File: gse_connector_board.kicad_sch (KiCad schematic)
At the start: 19 parts, among them J1 arming_connector, J2 gse_com_connector, J3 chg_connector, U4 L7805, U7 ISO1044BD, U9 MCP2562-E-SN

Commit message: wip
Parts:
- removed BUS1: 43045-0800, Connector_Molex:Molex_Micro-Fit_3.0_43045-0800_2x04_P3.00mm_Horizontal, symbol Connector_Generic:Conn_02x04_Top_Bottom
- removed H3: MountingHole_Pad, MountingHole:MountingHole_3.2mm_M3_DIN965_Pad, symbol Mechanical:MountingHole_Pad
- added J4: Conn_02x03_Top_Bottom, Connector_Molex:Molex_Micro-Fit_3.0_43045-0600_2x03_P3.00mm_Horizontal, symbol Connector_Generic:Conn_02x03_Top_Bottom
- added J5: Conn_02x02_Top_Bottom, Connector_Molex:Molex_Micro-Fit_3.0_43045-0400_2x02_P3.00mm_Horizontal, symbol Connector_Generic:Conn_02x02_Top_Bottom
- JP4: footprint Connector_PinHeader_1.27mm:PinHeader_1x02_P1.27mm_Vertical -> Jumper:SolderJumper-2_P1.3mm_Bridged_RoundedPad1.0x1.5mm
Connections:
- net supply is gone; now on net main_voltage: J1.1 (Pin_1)
- net CAN_1+: now also J4.6 (Pin_6)
- net CAN_1-: now also J4.3 (Pin_3)
- net CHG: now also J4.4 (Pin_4)
- net GND: now also J4.1 (Pin_1), J4.2 (Pin_2)
- net arm: now also J5.3 (Pin_3), J5.4 (Pin_4)
- net disarm: now also J5.1 (Pin_1), J5.2 (Pin_2)
- net main_voltage: now also J4.5 (Pin_5)
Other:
- note removed: "critical can"

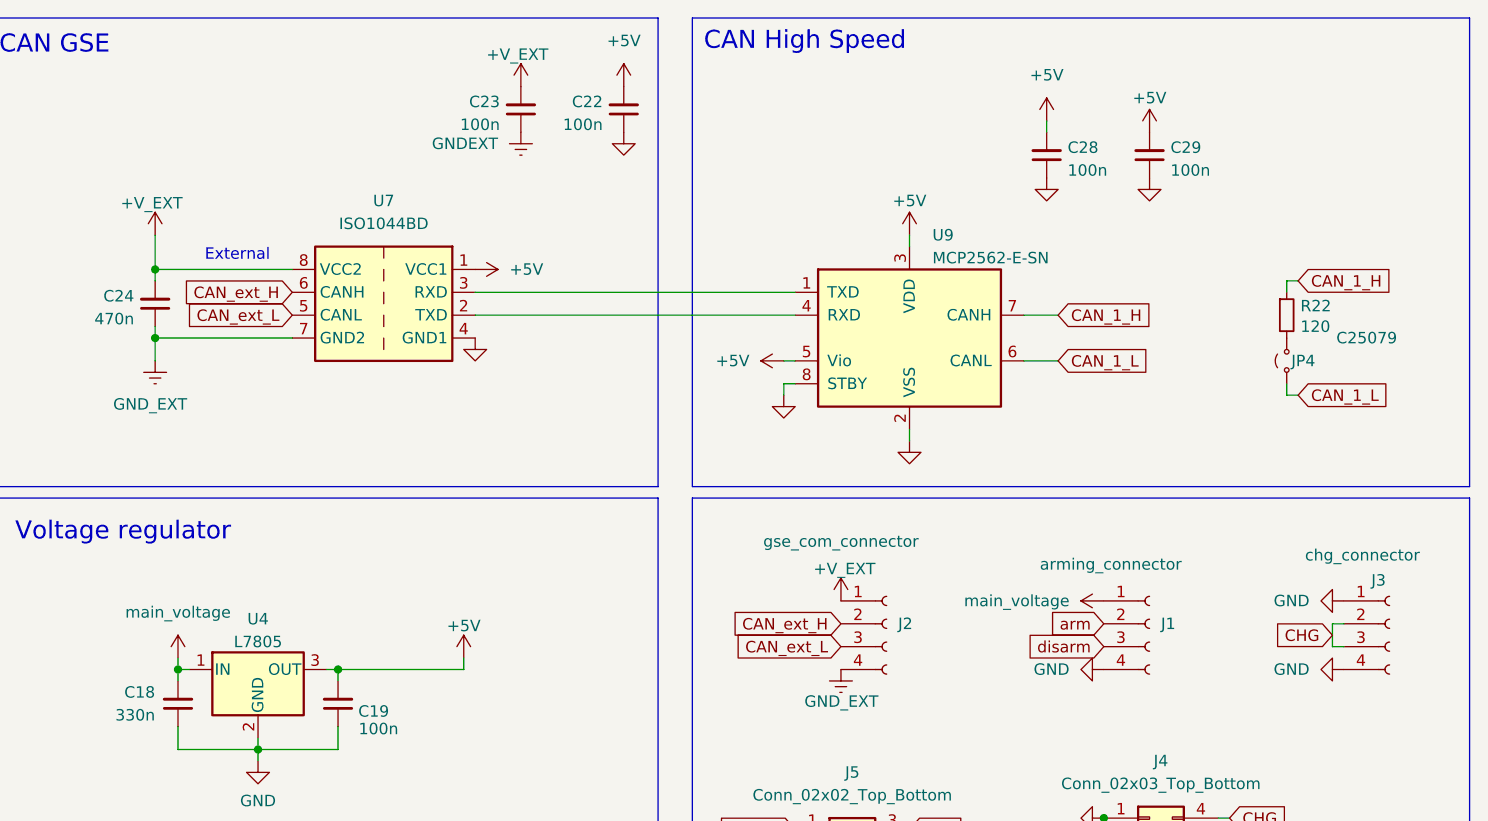
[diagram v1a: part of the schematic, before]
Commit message: Add files via upload
changed footprint of agnetic connector, finished routing and layout of connector board
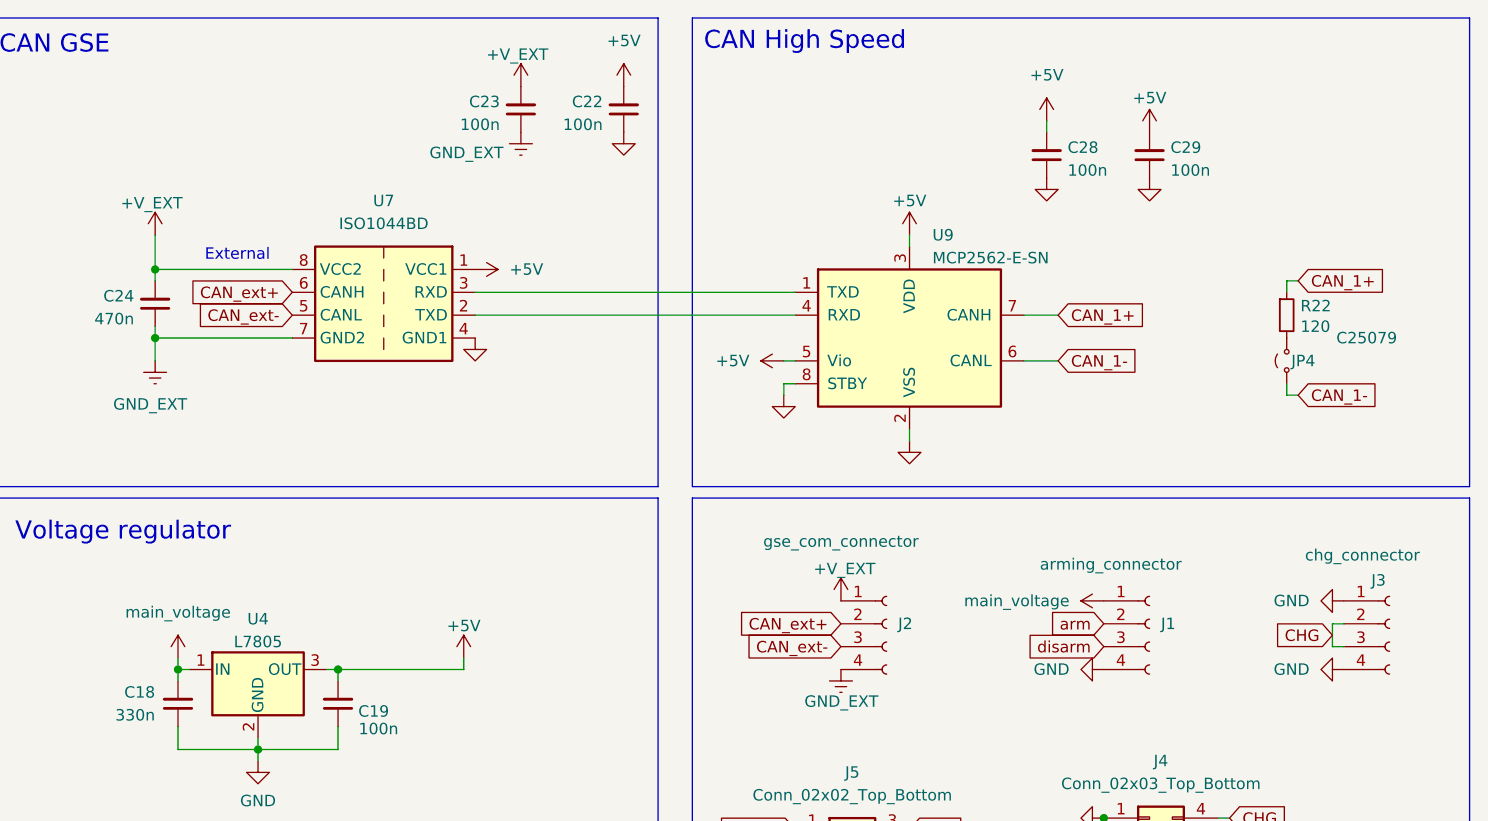
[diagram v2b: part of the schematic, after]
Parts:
- J1, J2, J3: footprint custom_parts:4_pin_mag_con -> custom_parts:4_pin_mag_con_new
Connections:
- net CAN_1_H is gone; now on net CAN_1+: R22.1, U9.7 (CANH)
- net CAN_1_L is gone; now on net CAN_1-: JP4.1 (A), U9.6 (CANL)
- net GNDEXT is gone; now on net GND_EXT: C23.1
- net CAN_ext_H renamed CAN_ext+
- net CAN_ext_L renamed CAN_ext-
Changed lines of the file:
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@@
 		)
 	)
-	(global_label "CAN_ext_H"
+	(global_label "CAN_ext+"
 		(shape input)
 		(at 111.76 82.55 180)
@@
 		)
 		(property "Intersheetrefs" "${INTERSHEET_REFS}"
-			(at 98.9776 82.55 0)
+			(at 99.7033 82.55 0)
 			(hide yes)
 			(show_name no)
@@
 		)
 	)
-	(global_label "CAN_1_L"
+	(global_label "CAN_1-"
 		(shape input)
 		(at 135.89 53.34 0)
@@
 		)
 		(property "Intersheetrefs" "${INTERSHEET_REFS}"
-			(at 146.7371 53.34 0)
+			(at 146.3138 53.34 0)
 			(hide yes)
 			(show_name no)
@@
 		)
 	)
-	(global_label "CAN_ext_H"
+	(global_label "CAN_ext+"
 		(shape input)
 		(at 50.8 45.72 180)
@@
 		)
 		(property "Intersheetrefs" "${INTERSHEET_REFS}"
-			(at 38.0176 45.72 0)
+			(at 38.7433 45.72 0)
 			(hide yes)
 			(show_name no)
@@
 		)
 	)
-	(global_label "CAN_1_H"
+	(global_label "CAN_1+"
 		(shape input)
 		(at 162.56 44.45 0)
@@
 		)
 		(property "Intersheetrefs" "${INTERSHEET_REFS}"
-			(at 173.7095 44.45 0)
+			(at 172.9838 44.45 0)
 			(hide yes)
 			(show_name no)
@@
 		)
 	)
-	(global_label "CAN_ext_L"
+	(global_label "CAN_ext-"
 		(shape input)
 		(at 50.8 48.26 180)
@@
 		)
 		(property "Intersheetrefs" "${INTERSHEET_REFS}"
-			(at 38.32 48.26 0)
+			(at 38.7433 48.26 0)
 			(hide yes)
 			(show_name no)
@@
 		)
 	)
-	(global_label "CAN_1_L"
+	(global_label "CAN_1-"
 		(shape input)
 		(at 162.56 57.15 0)
@@
 		)
 		(property "Intersheetrefs" "${INTERSHEET_REFS}"
-			(at 173.4071 57.15 0)
+			(at 172.9838 57.15 0)
 			(hide yes)
 			(show_name no)
@@
 		)
 	)
-	(global_label "CAN_ext_L"
+	(global_label "CAN_ext-"
 		(shape input)
 		(at 111.76 85.09 180)
@@
 		)
 		(property "Intersheetrefs" "${INTERSHEET_REFS}"
-			(at 99.28 85.09 0)
+			(at 99.7033 85.09 0)
 			(hide yes)
 			(show_name no)
@@
 		)
 	)
-	(global_label "CAN_1_H"
+	(global_label "CAN_1+"
 		(shape input)
 		(at 135.89 48.26 0)
@@
 		)
 		(property "Intersheetrefs" "${INTERSHEET_REFS}"
-			(at 147.0395 48.26 0)
+			(at 146.3138 48.26 0)
 			(hide yes)
 			(show_name no)
@@
 			)
 		)
-		(property "Footprint" "custom_parts:4_pin_mag_con"
+		(property "Footprint" "custom_parts:4_pin_mag_con_new"
 			(at 172.72 82.55 0)
 			(hide yes)
@@
 			)
 		)
-		(property "Footprint" "custom_parts:4_pin_mag_con"
+		(property "Footprint" "custom_parts:4_pin_mag_con_new"
 			(at 146.05 82.55 0)
 			(hide yes)
@@
 			)
 		)
-		(property "Footprint" "custom_parts:4_pin_mag_con"
+		(property "Footprint" "custom_parts:4_pin_mag_con_new"
 			(at 116.84 82.55 0)
 			(hide yes)
@@
 		(in_pos_files yes)
 		(dnp no)
-		(fields_autoplaced yes)
 		(property "Reference" "#PWR052"
 			(at 76.2 34.29 0)
@@
 			)
 		)
-		(property "Value" "GNDEXT"
-			(at 73.66 29.2099 0)
+		(property "Value" "GND_EXT"
+			(at 66.04 30.226 0)
 			(show_name no)
 			(do_not_autoplace no)
@@
 					(size 1.27 1.27)
 				)
-				(justify left)
+				(justify right)
 			)
 		)

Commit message: Add files via upload
Added Silkscreen and Testpoints for CAN
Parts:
- added TP1, TP2, TP3, TP4, TP5, TP6: TestPoint, TestPoint:TestPoint_Pad_1.0x1.0mm, symbol Connector:TestPoint
- Ue1: renamed from U4; LCSC (none) -> C310413; LCSC# C310413 -> (none)
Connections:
- net CAN_1+: now also TP1.1
- net CAN_1-: now also TP2.1
- net CAN_ext+: now also TP3.1
- net CAN_ext-: now also TP4.1
- net at U7.3 (RXD), U9.1 (TXD): now also TP6.1
- net at U7.2 (TXD), U9.4 (RXD): now also TP5.1

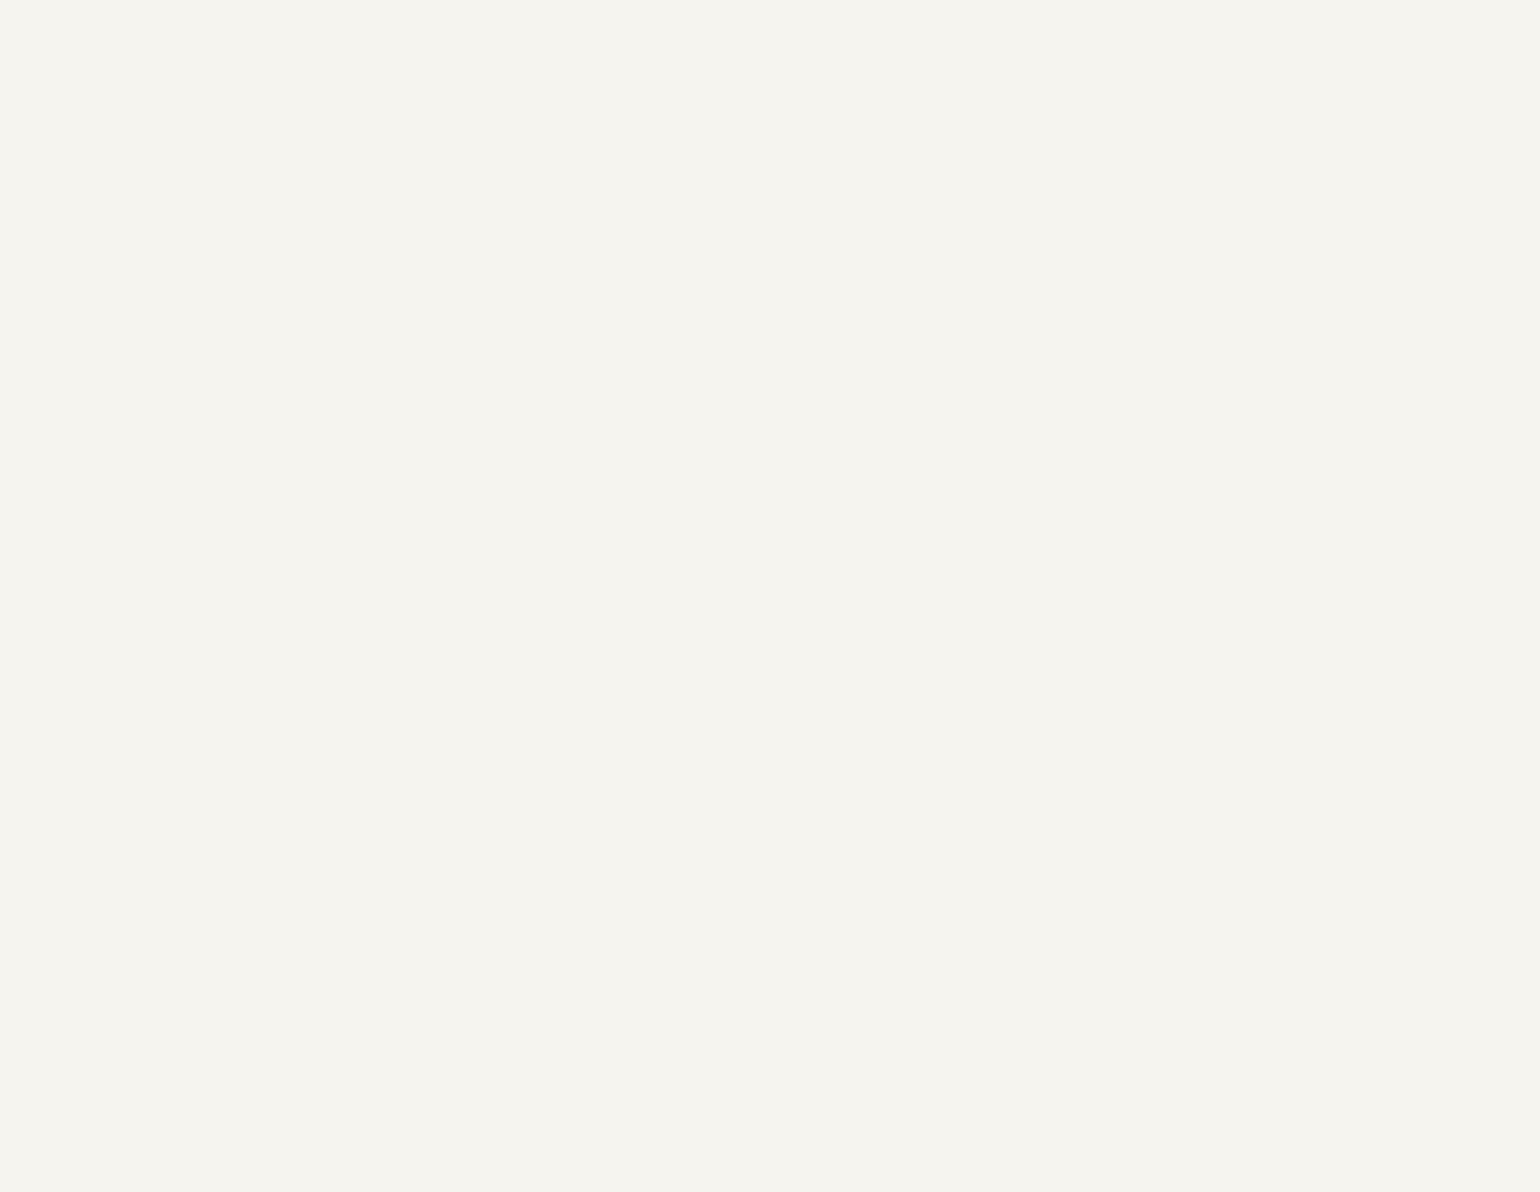
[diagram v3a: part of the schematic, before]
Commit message: Add files via upload
excluded Molex connectors from BOM and put in DNP.
added Testpoints for 5V, main voltage and Charging
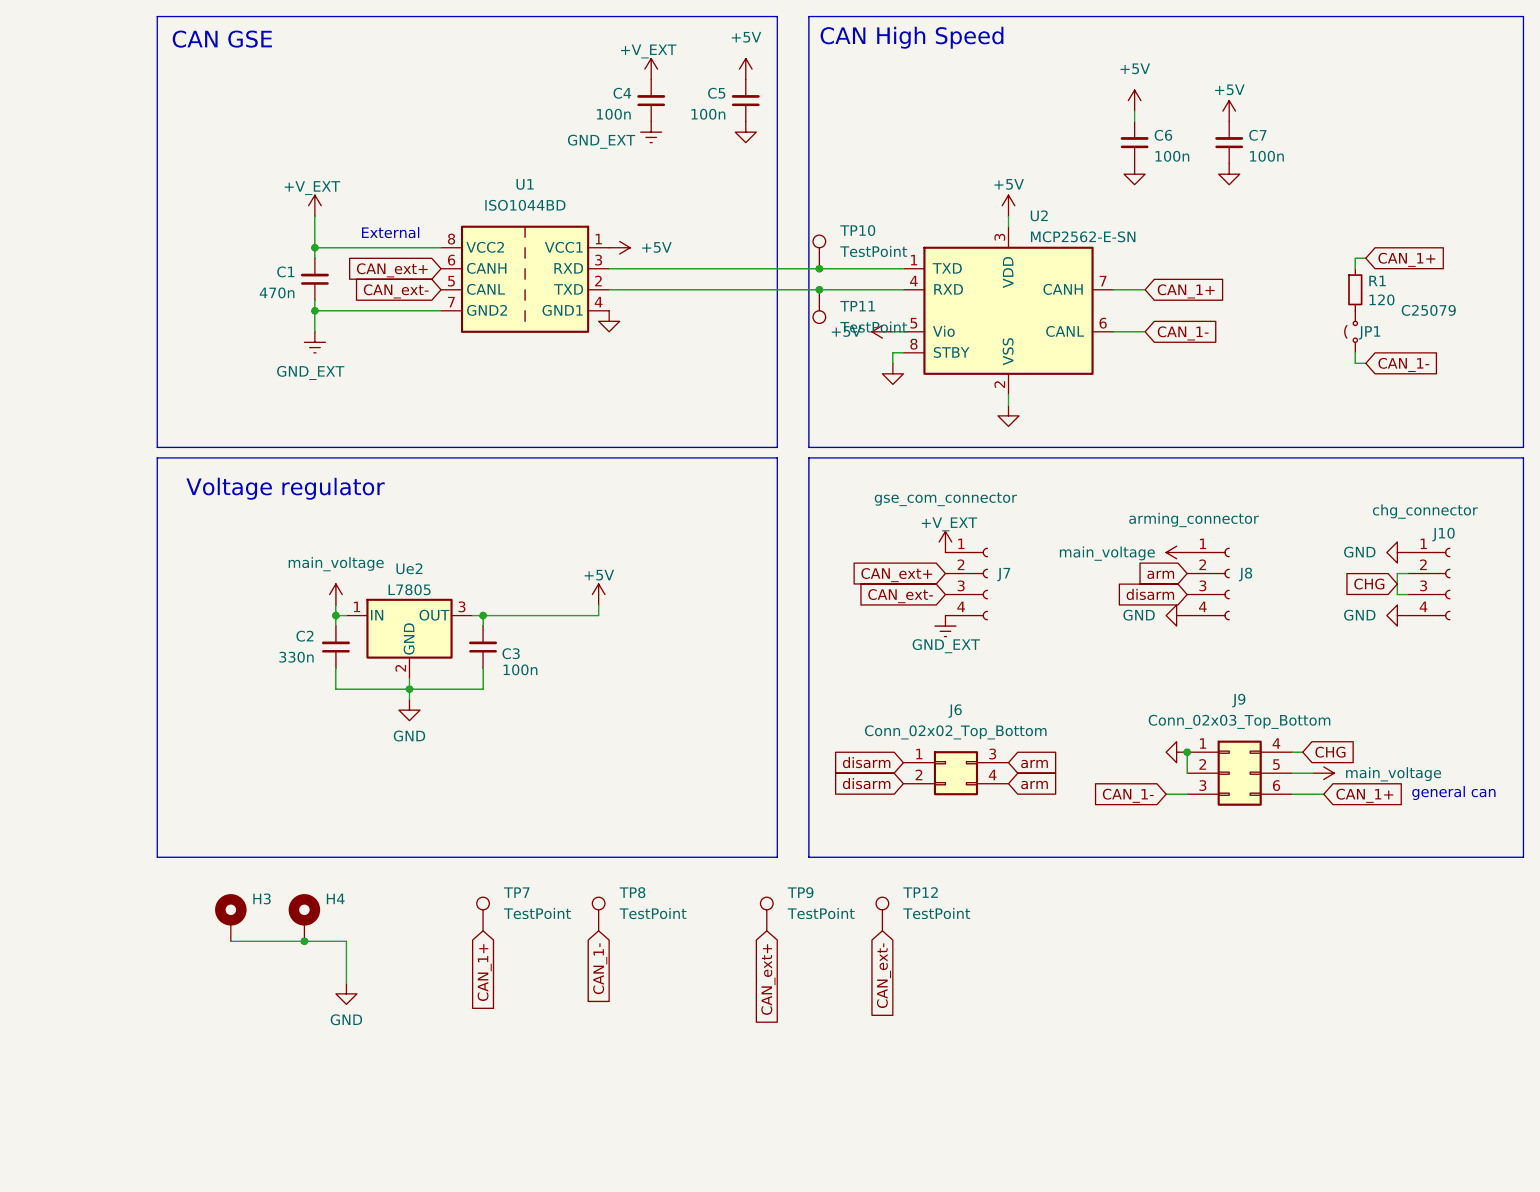
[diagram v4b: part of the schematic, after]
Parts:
- added C1: 470n, Capacitor_SMD:C_0603_1608Metric_Pad1.08x0.95mm_HandSolder, symbol Device:C_Small
- added C2: 330n, Capacitor_SMD:C_0603_1608Metric, symbol Device:C_Small
- added C3: 100n, Capacitor_SMD:C_0603_1608Metric, symbol Device:C_Small
- added C4, C5, C6, C7: 100n, Capacitor_SMD:C_0603_1608Metric_Pad1.08x0.95mm_HandSolder, symbol Device:C_Small
- added H3, H4: MountingHole_Pad, MountingHole:MountingHole_3.2mm_M3_DIN965_Pad, symbol Mechanical:MountingHole_Pad
- added J10: chg_connector, custom_parts:4_pin_mag_con_new, symbol Connector:Conn_01x04_Socket
- added J6: Conn_02x02_Top_Bottom, Connector_Molex:Molex_Micro-Fit_3.0_43045-0400_2x02_P3.00mm_Horizontal, symbol Connector_Generic:Conn_02x02_Top_Bottom
- added J7: gse_com_connector, custom_parts:4_pin_mag_con_new, symbol Connector:Conn_01x04_Socket
- added J8: arming_connector, custom_parts:4_pin_mag_con_new, symbol Connector:Conn_01x04_Socket
- added J9: Conn_02x03_Top_Bottom, Connector_Molex:Molex_Micro-Fit_3.0_43045-0600_2x03_P3.00mm_Horizontal, symbol Connector_Generic:Conn_02x03_Top_Bottom
- added JP1: Jumper_2_Small_Open, Jumper:SolderJumper-2_P1.3mm_Bridged_RoundedPad1.0x1.5mm, symbol Jumper:Jumper_2_Small_Open
- added R1: 120, Resistor_SMD:R_0402_1005Metric, symbol Device:R_Small
- added TP10, TP11, TP12, TP2, TP7, TP9: TestPoint, TestPoint:TestPoint_Pad_1.0x1.0mm, symbol Connector:TestPoint
- added U1: ISO1044BD, Package_SO:SOIC-8_3.9x4.9mm_P1.27mm, symbol Interface_CAN_LIN:ISO1044BD
- added U9: MCP2562-E-SN, Package_SO:SOIC-8_3.9x4.9mm_P1.27mm, symbol Interface_CAN_LIN:MCP2562-E-SN
- added Ue2: L7805, Package_TO_SOT_SMD:TO-252-2, symbol Regulator_Linear:L7805
- renumbered TP2 to TP8, U9 to U2
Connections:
- net +5V: now also C3.2, C5.2, C6.2, C7.2, U1.1 (VCC1), U9.3 (VDD), U9.5 (Vio), Ue2.3 (OUT)
- net +V_EXT: now also C1.2, C4.2, J7.1 (Pin_1), U1.8 (VCC2)
- net CAN_1+: now also J9.6 (Pin_6), R1.1, TP7.1, U9.7 (CANH)
- net CAN_1-: now also J9.3 (Pin_3), JP1.1 (A), TP2.1, U9.6 (CANL)
- net CAN_ext+: now also J7.2 (Pin_2), TP9.1, U1.6 (CANH)
- net CAN_ext-: now also J7.3 (Pin_3), TP12.1, U1.5 (CANL)
- net CHG: now also J10.2 (Pin_2), J10.3 (Pin_3), J9.4 (Pin_4)
- net GND: now also C2.1, C3.1, C5.1, C6.1, C7.1, H3.1, H4.1, J10.1 (Pin_1), J10.4 (Pin_4), J8.4 (Pin_4), J9.1 (Pin_1), J9.2 (Pin_2), U1.4 (GND1), U9.2 (VSS), U9.8 (STBY), Ue2.2 (GND)
- net GND_EXT: now also C1.1, C4.1, J7.4 (Pin_4), U1.7 (GND2)
- net arm: now also J6.3 (Pin_3), J6.4 (Pin_4), J8.2 (Pin_2)
- net disarm: now also J6.1 (Pin_1), J6.2 (Pin_2), J8.3 (Pin_3)
- net main_voltage: now also C2.2, J8.1 (Pin_1), J9.5 (Pin_5), Ue2.1 (IN)
- net at TP6.1, U7.3 (RXD): now also U9.1 (TXD); no longer U2.1 (TXD)
- net at TP5.1, U7.2 (TXD): now also U9.4 (RXD); no longer U2.4 (RXD)
- new net: TP10.1, U1.3 (RXD), U2.1 (TXD)
- new net: TP11.1, U1.2 (TXD), U2.4 (RXD)
- new net: JP1.2 (B), R1.2
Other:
- moved on the sheet: TP8, U2

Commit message: final silkscreen improvements and small fixes
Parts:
- removed C1: 470n, Capacitor_SMD:C_0603_1608Metric_Pad1.08x0.95mm_HandSolder, symbol Device:C_Small
- removed C2: 330n, Capacitor_SMD:C_0603_1608Metric, symbol Device:C_Small
- removed C3: 100n, Capacitor_SMD:C_0603_1608Metric, symbol Device:C_Small
- removed C4, C5, C6, C7: 100n, Capacitor_SMD:C_0603_1608Metric_Pad1.08x0.95mm_HandSolder, symbol Device:C_Small
- removed H3, H4: MountingHole_Pad, MountingHole:MountingHole_3.2mm_M3_DIN965_Pad, symbol Mechanical:MountingHole_Pad
- removed J10: chg_connector, custom_parts:4_pin_mag_con_new, symbol Connector:Conn_01x04_Socket
- removed J6: Conn_02x02_Top_Bottom, Connector_Molex:Molex_Micro-Fit_3.0_43045-0400_2x02_P3.00mm_Horizontal, symbol Connector_Generic:Conn_02x02_Top_Bottom
- removed J7: gse_com_connector, custom_parts:4_pin_mag_con_new, symbol Connector:Conn_01x04_Socket
- removed J8: arming_connector, custom_parts:4_pin_mag_con_new, symbol Connector:Conn_01x04_Socket
- removed J9: Conn_02x03_Top_Bottom, Connector_Molex:Molex_Micro-Fit_3.0_43045-0600_2x03_P3.00mm_Horizontal, symbol Connector_Generic:Conn_02x03_Top_Bottom
- removed JP1: Jumper_2_Small_Open, Jumper:SolderJumper-2_P1.3mm_Bridged_RoundedPad1.0x1.5mm, symbol Jumper:Jumper_2_Small_Open
- removed R1: 120, Resistor_SMD:R_0402_1005Metric, symbol Device:R_Small
- removed TP10, TP11, TP12, TP8, TP9: TestPoint, TestPoint:TestPoint_Pad_1.0x1.0mm, symbol Connector:TestPoint
- removed U1: ISO1044BD, Package_SO:SOIC-8_3.9x4.9mm_P1.27mm, symbol Interface_CAN_LIN:ISO1044BD
- removed U2: MCP2562-E-SN, Package_SO:SOIC-8_3.9x4.9mm_P1.27mm, symbol Interface_CAN_LIN:MCP2562-E-SN
- removed Ue2: L7805, Package_TO_SOT_SMD:TO-252-2, symbol Regulator_Linear:L7805
- C18, C19: footprint Capacitor_SMD:C_0603_1608Metric -> Capacitor_SMD:C_0603_1608Metric_Pad1.08x0.95mm_HandSolder
- R22: footprint Resistor_SMD:R_0402_1005Metric -> Resistor_SMD:R_0603_1608Metric_Pad0.98x0.95mm_HandSolder; LCSC C25079 -> C22787; Part# RC0603FR-07120RL -> (none)
- TP1, TP2, TP3, TP4, TP5, TP6, TP7: footprint TestPoint:TestPoint_Pad_1.0x1.0mm -> TestPoint:TestPoint_Pad_D1.0mm
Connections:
- net +5V: now also TP7.1
- net CAN_1+: no longer TP7.1
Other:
- moved on the sheet: TP5, TP6
